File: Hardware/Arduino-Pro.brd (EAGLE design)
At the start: 52.1 x 53.3 mm, 37 parts, among them J1 Digital, J2 Analog, J4 POWER, Q1 RESONATORSMD, U1 ATMEGA328, U2 3.3V

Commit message: Finished design review and checklist
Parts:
- added FRAME2: FRAME-LETTER, SparkFun-Aesthetics:CREATIVE_COMMONS
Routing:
- net RAW: track 24.1 -> 23.4 mm
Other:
- board text added: "Revised by: Marshall Taylor"
- board text added: "v17"
- board text removed: "12-20-11"
- board text removed: "Arduino Pro"
- board text removed: "Released under the Creative Commons Attribution Share-Alike 3.0 License"
- board text removed: "http://creativecommons.org/licenses/by-sa/3.0"

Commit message: Fixed schematic issues
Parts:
- Q1: value RESONATORSMD -> 8/16MHz
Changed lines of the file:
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@@
 <layer number="112" name="tSilk" color="7" fill="1" visible="no" active="yes"/>
 <layer number="113" name="IDFDebug" color="4" fill="1" visible="no" active="yes"/>
-<layer number="114" name="Badge_Outline" color="7" fill="1" visible="yes" active="yes"/>
-<layer number="115" name="ReferenceISLANDS" color="7" fill="1" visible="yes" active="yes"/>
+<layer number="114" name="Badge_Outline" color="7" fill="1" visible="no" active="yes"/>
+<layer number="115" name="ReferenceISLANDS" color="7" fill="1" visible="no" active="yes"/>
 <layer number="116" name="Patch_BOT" color="9" fill="4" visible="no" active="yes"/>
-<layer number="118" name="Rect_Pads" color="7" fill="1" visible="yes" active="yes"/>
+<layer number="118" name="Rect_Pads" color="7" fill="1" visible="no" active="yes"/>
 <layer number="121" name="_tsilk" color="7" fill="1" visible="no" active="yes"/>
 <layer number="122" name="_bsilk" color="7" fill="1" visible="no" active="yes"/>
@@
 <attribute name="PROD_ID" value="RES-07856" x="46.99" y="43.18" size="1.778" layer="27" rot="R270" display="off"/>
 </element>
-<element name="Q1" library="SparkFun" package="RESONATOR-SMD" value="RESONATORSMD" x="33.02" y="22.86">
+<element name="Q1" library="SparkFun" package="RESONATOR-SMD" value="8/16MHz" x="33.02" y="22.86">
 <attribute name="PROD_ID" value="XTAL-08900" x="33.02" y="22.86" size="1.778" layer="27" display="off"/>
 </element>

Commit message: Fixed more schematic issues
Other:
- board text added: "Original Arduino Mini Design by Team Arduino Arduino Pro Mini Design by SparkFun Electronics Revised by Pete Lewis and Marshall Taylor"
- board text removed: "Revised by: Marshall Taylor"
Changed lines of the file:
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@@
 <dimension x1="0" y1="0" x2="0" y2="53.34" x3="-29.21" y3="26.67" textsize="1.778" textratio="15" layer="47" dtype="vertical" unit="inch" visible="yes"/>
 <dimension x1="0" y1="0" x2="52.07" y2="0" x3="26.035" y3="-15.24" textsize="1.778" textratio="15" layer="47" dtype="horizontal" unit="inch" visible="yes"/>
-<text x="6.35" y="-31.75" size="1.778" layer="51" font="vector">Revised by: Marshall Taylor</text>
 <circle x="40.64" y="20.32" radius="0.179603125" width="0.381" layer="21"/>
+<text x="27.94" y="-29.21" size="1.778" layer="51" font="vector" ratio="9" align="top-left">Original Arduino Mini Design by Team Arduino
+Arduino Pro Mini Design by SparkFun Electronics
+Revised by Pete Lewis and Marshall Taylor</text>
 </plain>
 <attributes>
@@
 <attribute name="NAME" x="20.209" y="10.16" size="0.4064" layer="25" rot="R90"/>
 <attribute name="VALUE" x="20.982" y="12.508" size="0.4064" layer="27"/>
+<attribute name="PROD_ID" value="CAP-00811" x="21.59" y="12.7" size="1.778" layer="27" rot="R90" display="off"/>
 </element>
 <element name="U$3" library="SparkFun" package="STAND-OFF" value="STAND-OFF" x="2.54" y="2.54"/>
@@
 </board>
 </drawing>
+<compatibility>
+<note version="6.3" minversion="6.2.2" severity="warning">
+Since Version 6.2.2 text objects can contain more than one line,
+which will not be processed correctly with this version.
+</note>
+</compatibility>
 </eagle>

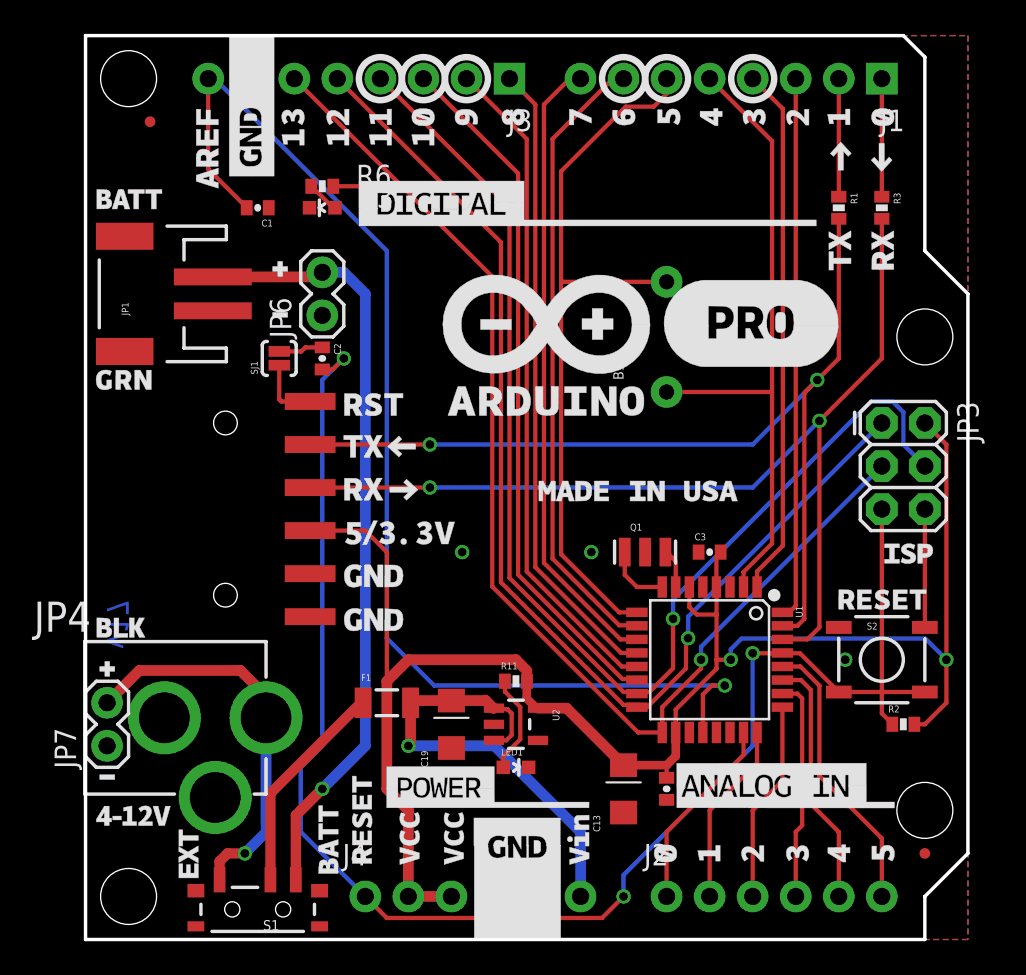
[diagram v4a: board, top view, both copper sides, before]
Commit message: Re-imported silk graphics, removed two-pin silk outlines, incremented rev number to 1.8
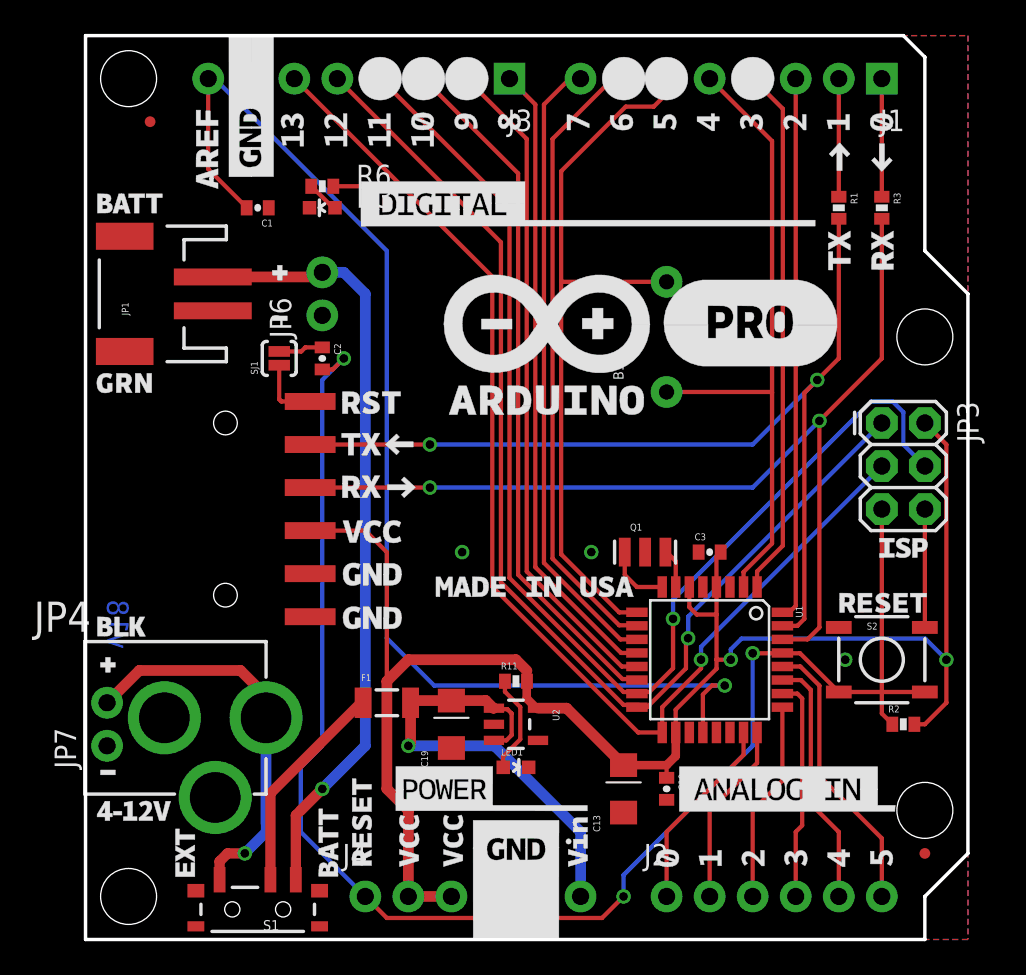
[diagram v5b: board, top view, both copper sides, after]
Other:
- board text added: "(Add these comments when uploading gerbers.)"
- board text added: "Blue soldermask: about 0% Red, 39% Green, 59% Blue. (Hex code: #006496)"
- board text added: "Ordering Instructions:"
- board text added: "v18"
- board text removed: "v17"

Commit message: Post review and checklist verification
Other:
- board text added: "Blue soldermask: Screen color: 0% Red, 39% Green, 59% Blue. (Hex code: #006496) Pantone: 308 C / 315 U"
- board text removed: "Blue soldermask: about 0% Red, 39% Green, 59% Blue. (Hex code: #006496)"

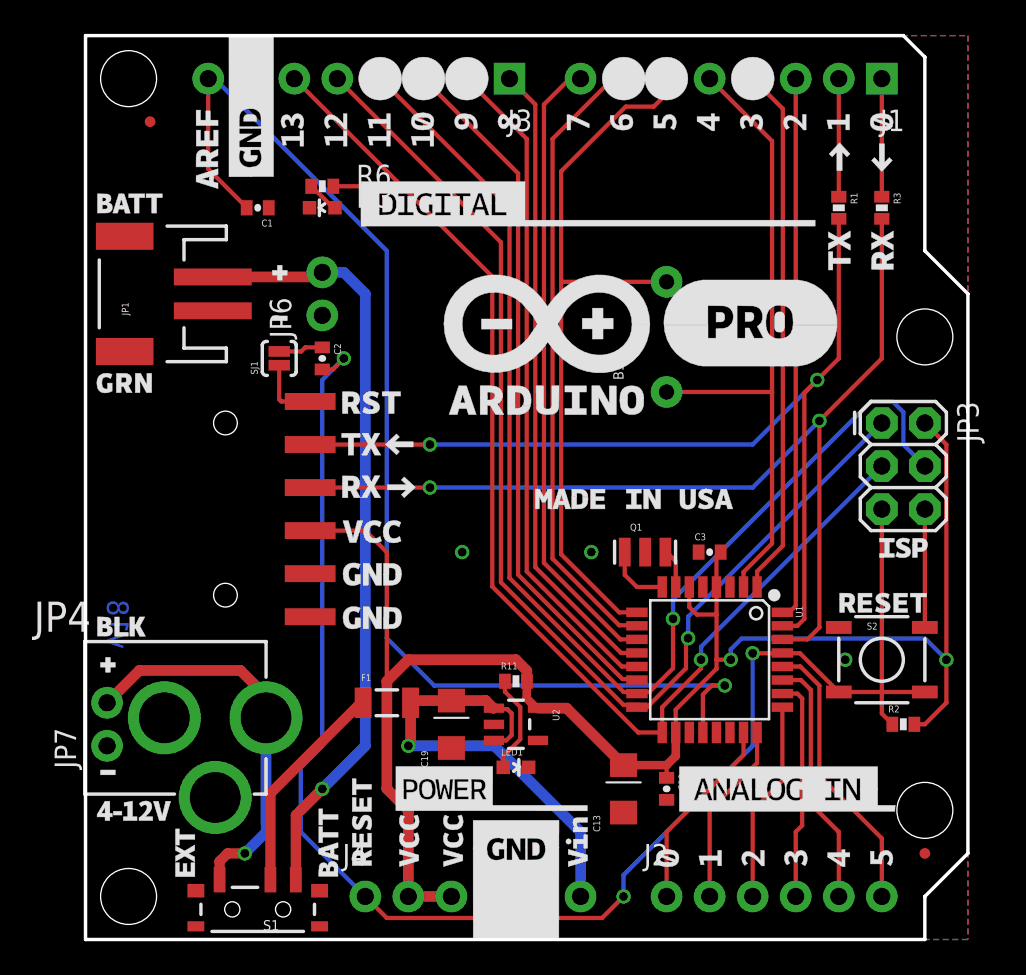
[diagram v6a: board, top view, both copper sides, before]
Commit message: Enlarged circles, incremented version number
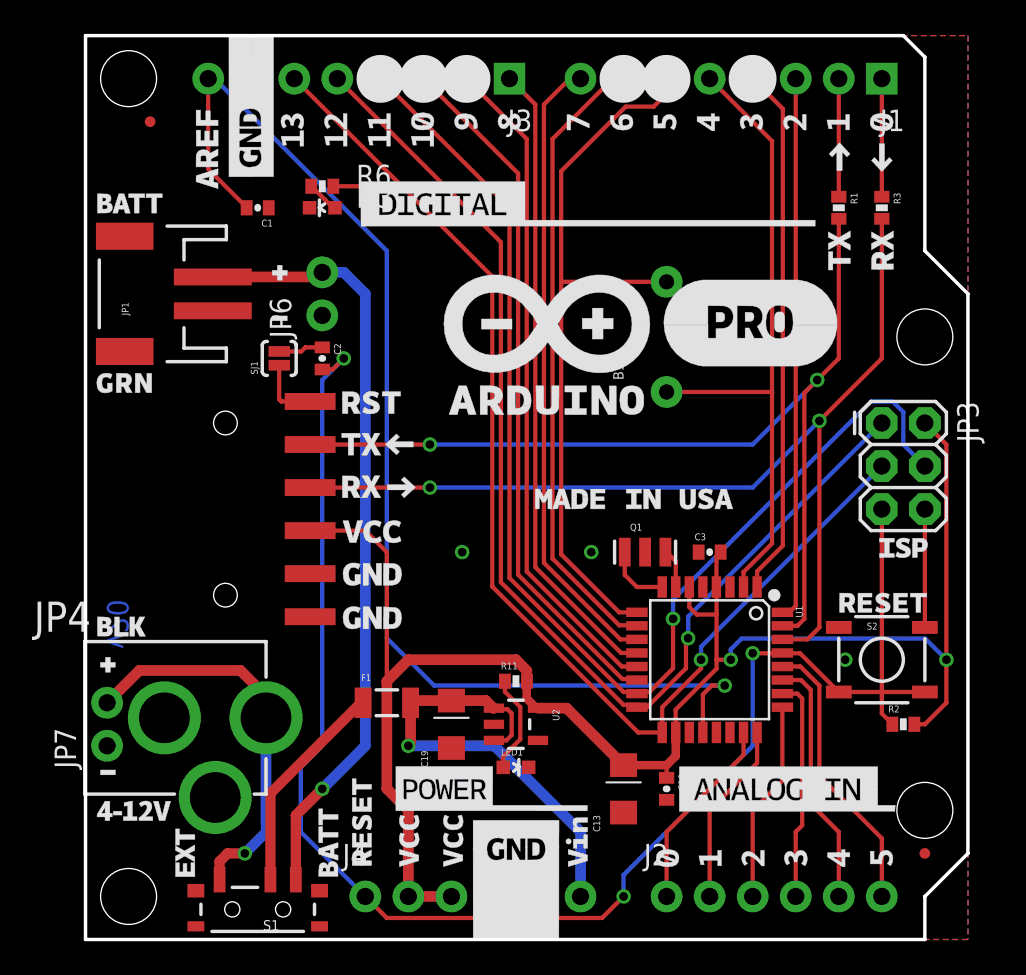
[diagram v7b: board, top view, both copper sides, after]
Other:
- board text added: "v20"
- board text removed: "v18"
